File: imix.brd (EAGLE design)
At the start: 87 x 102.5 mm, 151 parts, among them Q2 AO3415, Q3 AO3415, Q4 AO3415, Q5 AO3415, U1 BQ2423X, U10 ISL29035, U11 FX0S8700CQ, U12 296-12686-1-ND, U3 TLV3202, U4 LM358, U5 LDO-TPS78233, U6 ATSAM4LCX_100, U8 SI7021, U9 NRF51822, X1 16MHz, X2 16MHz, X3 16MHz

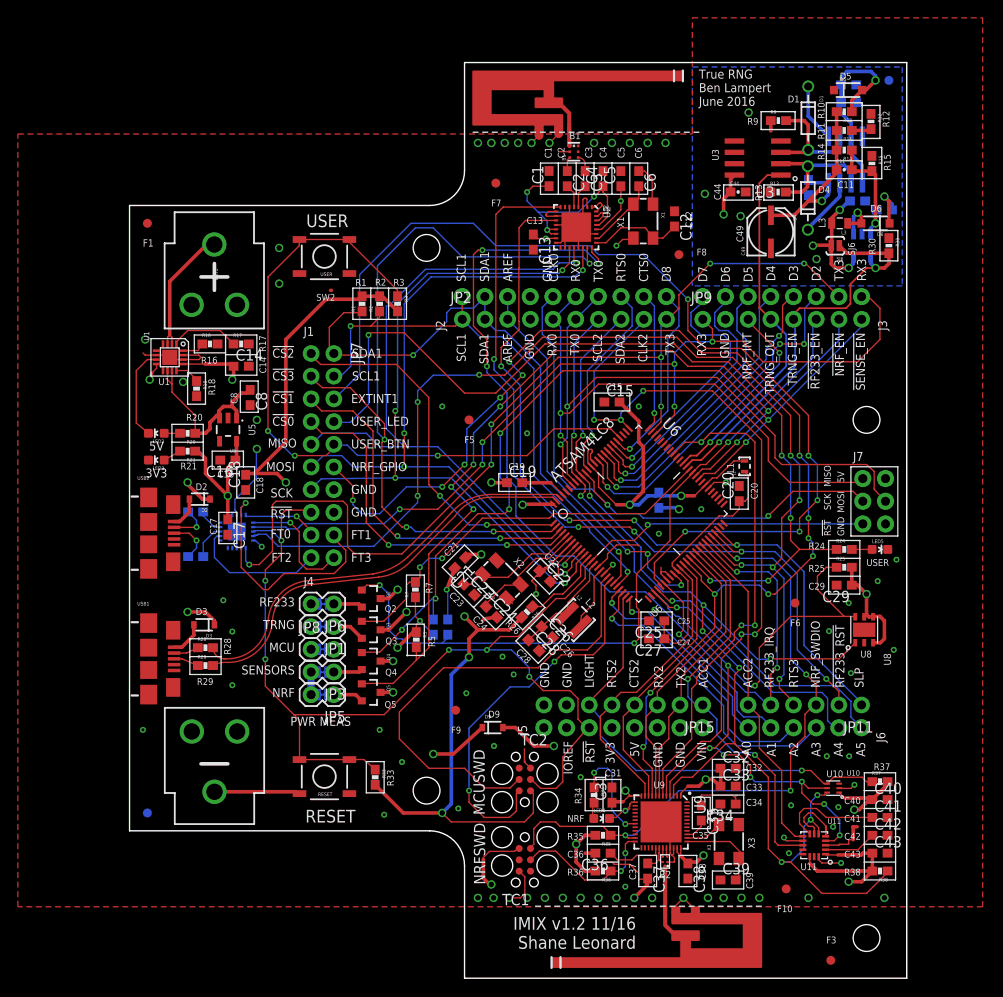
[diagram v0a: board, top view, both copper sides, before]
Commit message: Improve schematic readability and update PDF docs: Fixes #10
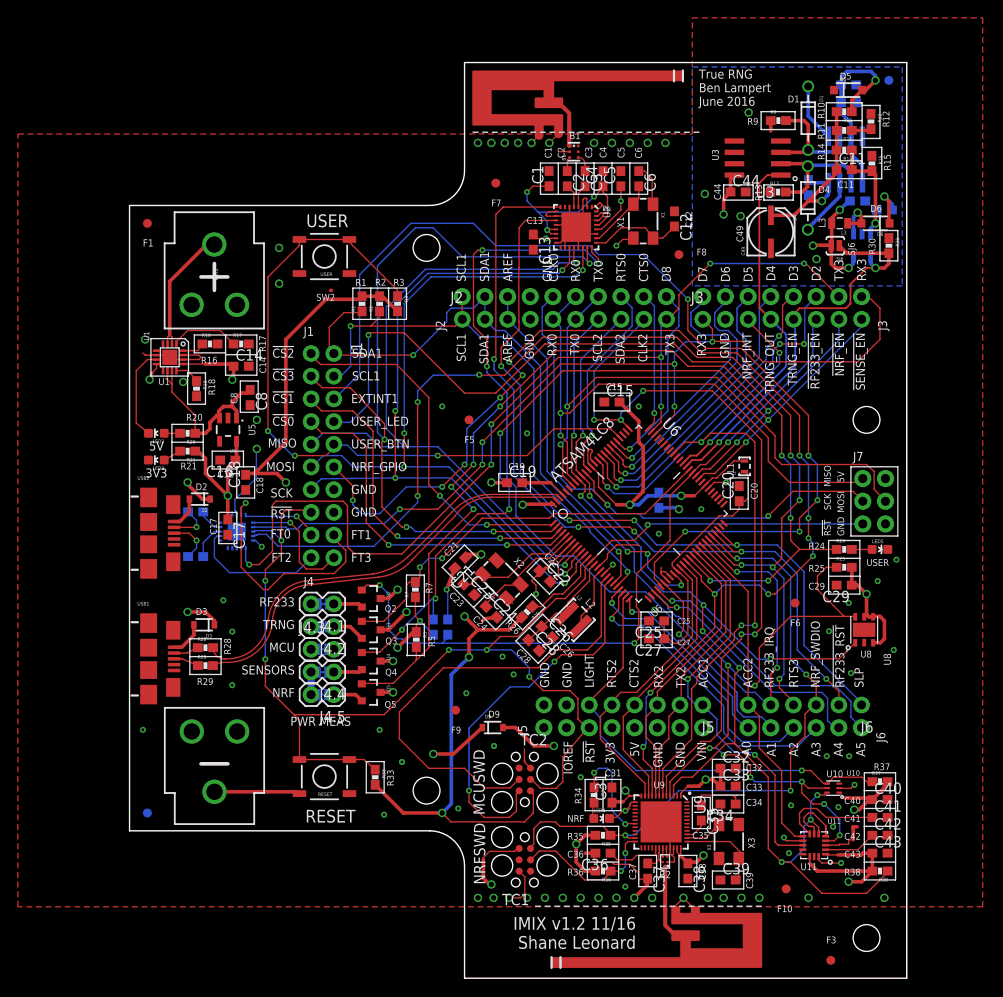
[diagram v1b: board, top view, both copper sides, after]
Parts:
- C1, C12, C13, C14, C15, C16, C18, C19, C2, C20, C21, C22, C23, C24, C25, C26, C27, C28, C29, C3, C31, C32, C33, C34, C35, C36, C37, C38, C39, C4, C40, C41, C42, C43, C5, C50, C6, C8: device rcl:C0603 -> imix:C0603
- C11, C44, C47, C48, C7: device SparkFun-Capacitors:0603-CAP -> imix:C0603
- C45, C46: device SparkFun-Passives:0603-CAP -> imix:C0603
- C49: device SparkFun-Capacitors:PANASONIC_C -> imix:PANASONIC_C
- R1, R16, R17, R18, R2, R20, R21, R22, R23, R24, R25, R26, R28, R29, R3, R33, R34, R35, R36, R37, R38, R4, R5, R6, R7: device SparkFun-Passives:0603-RES -> imix:0603-RES
- R10, R11, R12, R13, R14, R15, R30, R9: device SparkFun-Resistors:0603-RES -> imix:0603-RES
- U9: value NRF51822 -> NRF51422
- renumbered JP1 to J4.2, JP11 to J6, JP15 to J5, JP2 to J2, JP3 to J4.4, JP4 to J2_3_5_AND_6, JP5 to J4.5, JP6 to J4.1, JP7 to J1, JP8 to J4.3, JP9 to J3

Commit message: Connect SAM4L pin 8 and 97 to VDDIO and reduce RNG ground plane: addresses #7 and #9
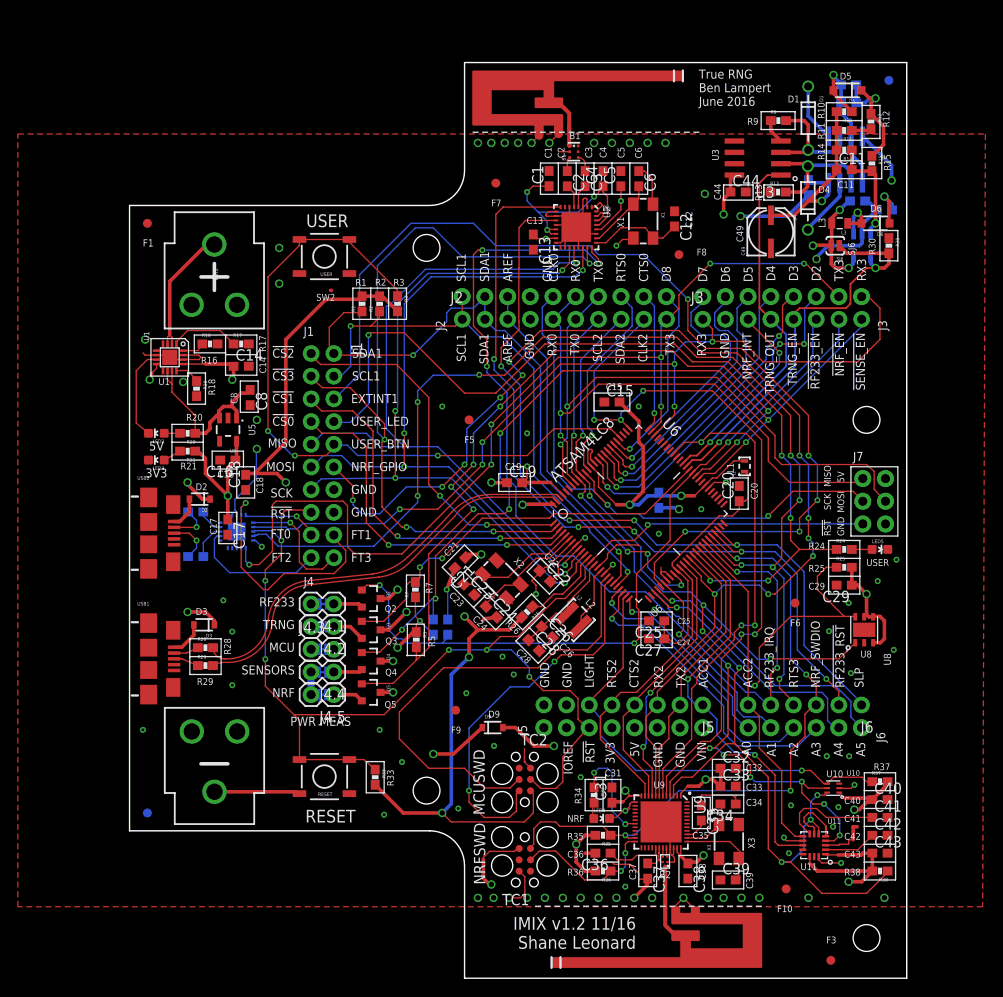
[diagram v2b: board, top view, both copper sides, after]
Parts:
- moved D5 0.08 mm to (80.4, 82.9), turned to 180 degrees
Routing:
- net GND: track 187.9 -> 219.8 mm, vias 83 -> 84
- net N$66: track 22.6 -> 18.5 mm
- net VCC_MCU_3V3: track 184.9 -> 188.3 mm, vias 8 -> 10
- removed copper zone on layer 16, net GND
